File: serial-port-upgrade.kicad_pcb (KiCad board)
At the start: 2 copper layers, 19 x 46.7 mm, 12 parts, among them J1 MFP 7 RC, J2 MFP 11 VCC, J3 MFP 16 TDO, J4 MFP 18 XTAL2, J5 MFP 34 /IEI, J6 MFP 36 GND, SW1 MOD ENABLE, U1 4040

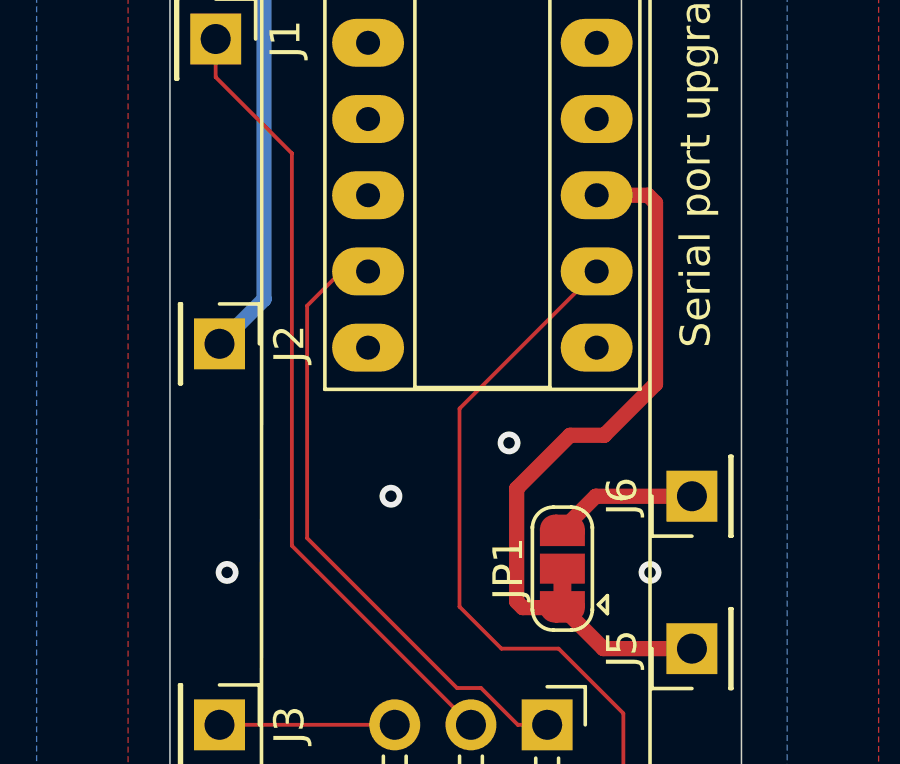
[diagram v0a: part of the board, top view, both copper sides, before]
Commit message: adjusted copper pour parameters
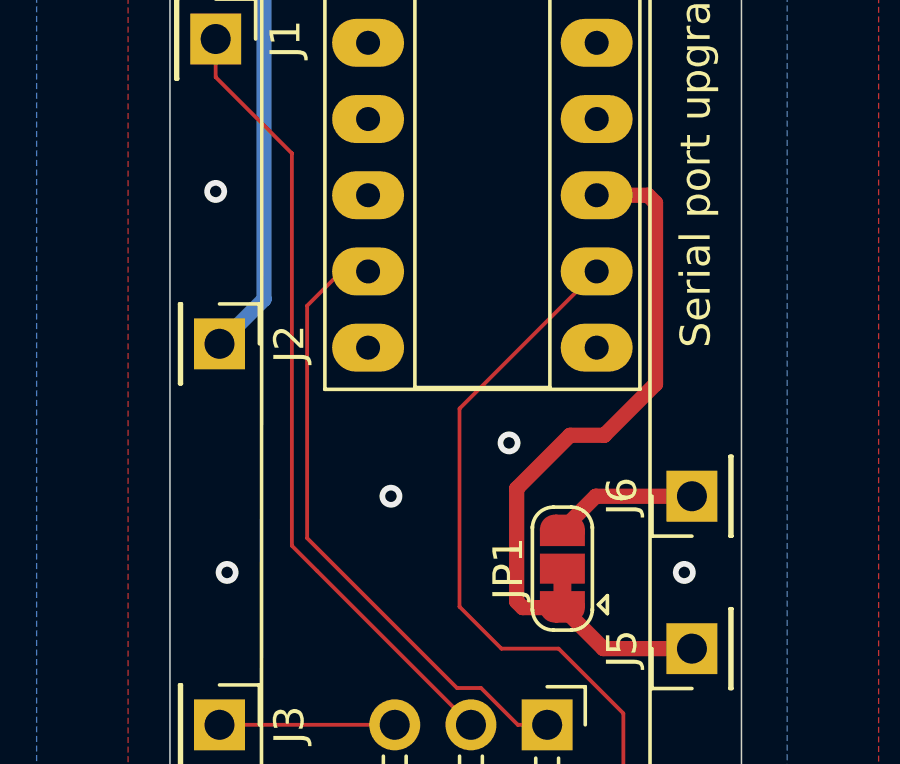
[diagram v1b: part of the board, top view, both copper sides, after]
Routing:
- net /mod_gnd: vias 3 -> 7
- net (no net): vias 3 -> 0
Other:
- net class POWER: clearance 0.508 -> 0.127

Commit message: latest details, gallery
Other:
- board text added: "38k4 bps"
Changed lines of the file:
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@@
   (general
     (thickness 1.6)
-    (drawings 20)
+    (drawings 21)
     (tracks 48)
     (zones 0)
@@
       (net 2 "Net-(C1-Pad1)"))
   )
+  (gr_text "38k4 bps\n" (at 91.313 146.177 90) (layer F.SilkS)
+    (effects (font (size 1 1) (thickness 0.15)) (justify left))
+  )
   (gr_text "MFP 1" (at 76.2 104.902 90) (layer F.SilkS)
     (effects (font (size 1 1) (thickness 0.15)))
@@
   (via (at 76.2 134.62) (size 0.762) (drill 0.381) (layers F.Cu B.Cu) (net 1))
   (via (at 76.581 142.24) (size 0.762) (drill 0.381) (layers F.Cu B.Cu) (net 1))
-  (via (at 91.567 142.621) (size 0.762) (drill 0.381) (layers F.Cu B.Cu) (net 1))
+  (via (at 91.948 142.113) (size 0.762) (drill 0.381) (layers F.Cu B.Cu) (net 1))
   (via (at 91.44 134.62) (size 0.762) (drill 0.381) (layers F.Cu B.Cu) (net 1))
   (via (at 85.598 130.302) (size 0.762) (drill 0.381) (layers F.Cu B.Cu) (net 1))
